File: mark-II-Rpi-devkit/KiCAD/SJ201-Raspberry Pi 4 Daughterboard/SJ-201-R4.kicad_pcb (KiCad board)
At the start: 4 copper layers, 67 x 98 mm, 205 parts, among them J1 Barrel_Jack, J10 Debug Connector, J12 FanConnector, J13 USB-PinHeader, J2 USB_C, J3 SPK, J4 SPK, J5 PowerTP, J6 Raspberry_Pi_4, J9 AudioJack3_Ground_Switch, Q3 AO3401A, SW1 MuteMic, U1 XL4501E1, U10 SPK0641HT4H-1, U11 SPK0641HT4H-1, U12 TPS75933KTT, U13 ATtiny1614-SS, U14 NC7NZ34K8XTR, U2 CoralTPU, U3 TAS5806MD, U4 AMS1117-3.3, U5 SN74LVC125APWR, U6 FE1.1s, U7 MP2359, U8 XMOS-XVF3510, U9 AT25SF161 16MBIT, X1 SG-210STF 24M, Y2 12MHz

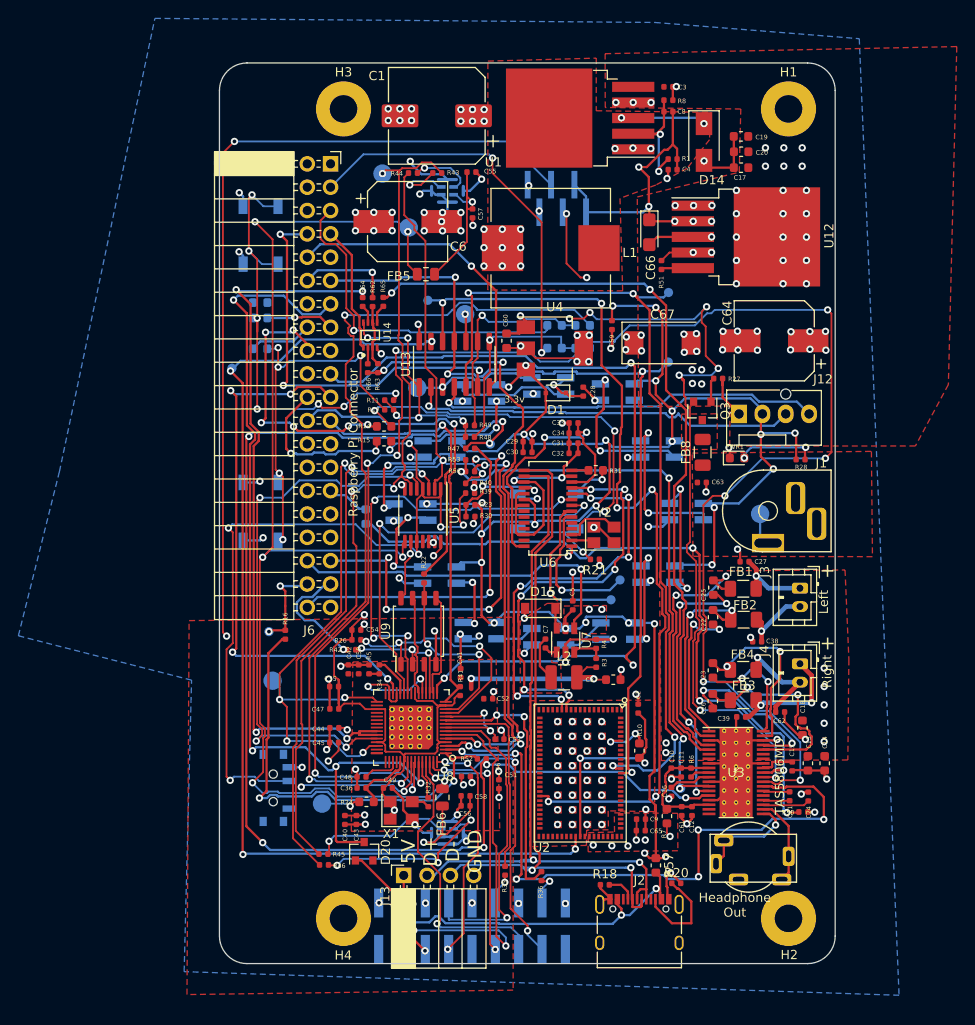
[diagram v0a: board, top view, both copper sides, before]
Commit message: Rev4 Update - fix some wiring, export for printing Rev 4
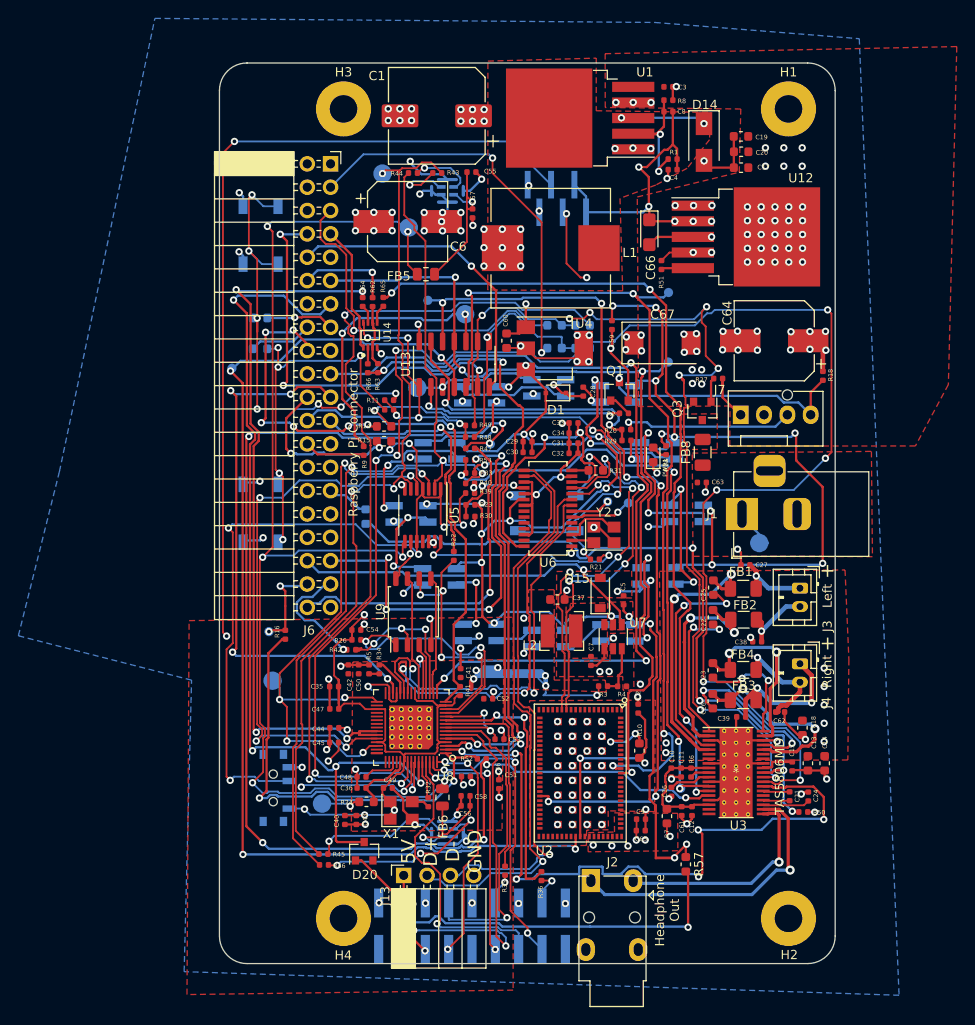
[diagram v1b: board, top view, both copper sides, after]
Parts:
- removed J12: FanConnector, Connector:FanPinHeader_1x04_P2.54mm_Vertical
- removed J9: AudioJack3_Ground_Switch, mycroft:STX-3790-5N
- removed R56: 0R - DNP, Resistor_SMD:R_0402_1005Metric
- added H6: MountingHole, libraries:simon-jestor-logo, B.Cu at (61.0, 30.4)
- added J7: FanConnector, Connector:FanPinHeader_1x04_P2.54mm_Vertical, F.Cu at (56.7, 38.3)
- added Q1: MMBT3904, Package_TO_SOT_SMD:SOT-23, F.Cu at (43.5, 35.7)
- added R2: 4.7k, Resistor_SMD:R_0402_1005Metric, F.Cu at (44.0, 38.1)
- added R29: 10k, Resistor_SMD:R_0402_1005Metric, F.Cu at (44.3, 41.1)
- added R33: 0R, Resistor_SMD:R_0402_1005Metric, F.Cu at (27.3, 44.6)
- J1: footprint user:BarrelJack_Vertical -> Connector_BarrelJack:BarrelJack_Horizontal
- J2: value USB_C -> AudioJack2_Ground; footprint Connector_USB:USB_C_Receptacle_XKB_U262-16XN-4BVC11 -> user:Jack_3.5mm_PJ-3210
- L2: value 2.2UH ±30% 1.55A -> 1.8UH ±30% 2.35A; footprint Inductor_SMD:L_1210_3225Metric -> Inductor_SMD:L_Bourns-SRN4018
- R18: value 5.1k -> 4.7k
- R20: value 5.1k -> 27k
- R3: value 75k -> 47k
- R4: value 330K -> 200k
- R9: value 0R -> 4.7k; footprint Resistor_SMD:R_0603_1608Metric -> Resistor_SMD:R_0402_1005Metric; moved to F.Cu
- moved R18 60.3 mm to (65.7, 34.0), turned to 270 degrees
- moved R20 49.7 mm to (44.3, 39.9), turned to 0 degrees
- moved H7 24.1 mm to (54.9, 74.0)
- moved R9 19.7 mm to (15.7, 42.2), turned to 90 degrees
- moved R28 14.7 mm to (48.6, 42.1), turned to 90 degrees
- moved DP3 10.7 mm to (42.2, 47.7)
- moved C37 10.6 mm to (36.8, 58.4)
- moved PWR1 9.13 mm to (47.2, 42.6), turned to 90 degrees
- moved DM3 8.43 mm to (44.5, 47.9)
- moved D15 6.73 mm to (41.4, 57.7), turned to 90 degrees
- moved J2 6.09 mm to (42.7, 100.0), turned to 180 degrees
- moved C5 5.56 mm to (44.0, 58.5)
- moved R4 5.40 mm to (43.8, 67.8), turned to 180 degrees
- moved C7 5.31 mm to (40.4, 65.1)
- moved U7 5.19 mm to (42.8, 62.4)
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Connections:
- J6 pad 26: (no net) -> ATtinyRESET
- R18 pad 1: GND -> PVDD
- R18 pad 2: Net-(J2-PadA5) -> /Monitor/FAN_PWM
- R20 pad 1: GND -> FanTach
- R20 pad 2: Net-(J2-PadB5) -> Net-(J7-Pad3)
- R9 pad 1: (no net) -> ATtinyRESET
- R9 pad 2: (no net) -> Net-(R9-Pad2)
- TP2 pad 1: Net-(TP2-Pad1) -> Net-(R9-Pad2)
- U13 pad 10: Net-(TP2-Pad1) -> Net-(R9-Pad2)
- U13 pad 13: TPU_PMIC_EN -> FanTach
- U13 pad 4: FanTemp -> TPU_PMIC_EN
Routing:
- net FanTemp: track 42.8 -> 0.00 mm, vias 1 -> 0
- net FanTach: track 0.00 -> 31.6 mm, vias 0 -> 2
- net Net-(R9-Pad2): track 0.00 -> 30.7 mm, vias 0 -> 2
- net +3V3: track 124.8 -> 154.8 mm, vias 33 -> 34
- net /Monitor/FAN_PWM: track 0.00 -> 28.6 mm, vias 0 -> 1
- net VoutL: track 9.65 -> 32.2 mm, vias 0 -> 1
- net FanPWM: track 42.9 -> 23.5 mm, vias 1 -> 2
- net Net-(J7-Pad3): track 0.00 -> 18.9 mm, vias 0 -> 1
- net +5V: track 245.6 -> 263.8 mm, vias 49 -> 45
- net /RaspberryPi/D-: track 75.5 -> 59.8 mm, vias 2 -> 1
- net /RaspberryPi/D+: track 76.9 -> 61.4 mm, vias 2 -> 1
- net Net-(DP3-Pad1): track 18.6 -> 4.33 mm
- net +1V0: track 164.0 -> 177.0 mm, vias 13 -> 17
- net VoutR: track 11.4 -> 23.9 mm
- net Net-(J2-PadB5): track 10.8 -> 0.00 mm
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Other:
- net class Audio added: clearance 0.09, trace_width 0.35, via_dia 1, via_drill 0.5
- board text removed: "3.3v"
